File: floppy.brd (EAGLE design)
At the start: 88.6 x 93.7 mm, 19 parts, among them IC1 ATTINY13-20SU, Q1 BC547

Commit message: Changed to 96HZ, added circle on back
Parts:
- L1: value ~250nH?? -> (none)
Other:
- board text added: "96"
- board text added: "Warning: Pirate radio transmitter"
- board text removed: "91"
- board text removed: "Warning: Pirate radio transmitter / #RevoltFM"
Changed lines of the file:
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@@
 <?xml version="1.0" encoding="utf-8"?>
 <!DOCTYPE eagle SYSTEM "eagle.dtd">
-<eagle version="7.7.0">
+<eagle version="8.3.1">
 <drawing>
 <settings>
 <setting alwaysvectorfont="no"/>
+<setting keepoldvectorfont="yes"/>
 <setting verticaltext="up"/>
 </settings>
@@
 <layer number="17" name="Pads" color="2" fill="1" visible="yes" active="yes"/>
 <layer number="18" name="Vias" color="2" fill="1" visible="yes" active="yes"/>
-<layer number="19" name="Unrouted" color="6" fill="1" visible="no" active="yes"/>
+<layer number="19" name="Unrouted" color="6" fill="1" visible="yes" active="yes"/>
 <layer number="20" name="Dimension" color="15" fill="1" visible="yes" active="yes"/>
-<layer number="21" name="tPlace" color="7" fill="1" visible="yes" active="yes"/>
+<layer number="21" name="tPlace" color="7" fill="1" visible="no" active="yes"/>
 <layer number="22" name="bPlace" color="7" fill="1" visible="yes" active="yes"/>
 <layer number="23" name="tOrigins" color="15" fill="1" visible="no" active="yes"/>
-<layer number="24" name="bOrigins" color="15" fill="1" visible="no" active="yes"/>
-<layer number="25" name="tNames" color="7" fill="1" visible="yes" active="yes"/>
-<layer number="26" name="bNames" color="7" fill="1" visible="no" active="yes"/>
-<layer number="27" name="tValues" color="7" fill="1" visible="yes" active="yes"/>
+<layer number="24" name="bOrigins" color="15" fill="1" visible="yes" active="yes"/>
+<layer number="25" name="tNames" color="7" fill="1" visible="no" active="yes"/>
+<layer number="26" name="bNames" color="7" fill="1" visible="yes" active="yes"/>
+<layer number="27" name="tValues" color="7" fill="1" visible="no" active="yes"/>
 <layer number="28" name="bValues" color="7" fill="1" visible="no" active="yes"/>
-<layer number="29" name="tStop" color="7" fill="3" visible="yes" active="yes"/>
-<layer number="30" name="bStop" color="7" fill="6" visible="yes" active="yes"/>
+<layer number="29" name="tStop" color="7" fill="3" visible="no" active="yes"/>
+<layer number="30" name="bStop" color="7" fill="6" visible="no" active="yes"/>
 <layer number="31" name="tCream" color="7" fill="4" visible="no" active="yes"/>
 <layer number="32" name="bCream" color="7" fill="5" visible="no" active="yes"/>
@@
 <layer number="38" name="bTest" color="7" fill="1" visible="no" active="yes"/>
 <layer number="39" name="tKeepout" color="4" fill="11" visible="no" active="yes"/>
-<layer number="40" name="bKeepout" color="1" fill="11" visible="no" active="yes"/>
+<layer number="40" name="bKeepout" color="1" fill="11" visible="yes" active="yes"/>
 <layer number="41" name="tRestrict" color="4" fill="10" visible="no" active="yes"/>
-<layer number="42" name="bRestrict" color="1" fill="10" visible="no" active="yes"/>
+<layer number="42" name="bRestrict" color="1" fill="10" visible="yes" active="yes"/>
 <layer number="43" name="vRestrict" color="2" fill="10" visible="no" active="yes"/>
 <layer number="44" name="Drills" color="7" fill="1" visible="no" active="yes"/>
-<layer number="45" name="Holes" color="7" fill="1" visible="no" active="yes"/>
+<layer number="45" name="Holes" color="7" fill="1" visible="yes" active="yes"/>
 <layer number="46" name="Milling" color="3" fill="1" visible="no" active="yes"/>
 <layer number="47" name="Measures" color="7" fill="1" visible="no" active="yes"/>
@@
 <layer number="49" name="Reference" color="7" fill="1" visible="no" active="yes"/>
 <layer number="50" name="dxf" color="7" fill="1" visible="no" active="yes"/>
-<layer number="51" name="tDocu" color="7" fill="1" visible="yes" active="yes"/>
-<layer number="52" name="bDocu" color="7" fill="1" visible="no" active="yes"/>
+<layer number="51" name="tDocu" color="7" fill="1" visible="no" active="yes"/>
+<layer number="52" name="bDocu" color="7" fill="1" visible="yes" active="yes"/>
 <layer number="90" name="Modules" color="5" fill="1" visible="no" active="no"/>
 <layer number="91" name="Nets" color="2" fill="1" visible="no" active="no"/>
@@
 </polygon>
 <text x="6.2484" y="89.154" size="4.0132" layer="21" font="vector" ratio="16" align="center">FM</text>
-<text x="6.2738" y="84.6074" size="4.064" layer="21" font="vector" ratio="15" align="center">91</text>
+<text x="6.2738" y="84.6074" size="4.064" layer="21" font="vector" ratio="15" align="center">96</text>
 <text x="6.0706" y="80.645" size="2.54" layer="21" font="vector" ratio="17" align="center">MHz</text>
 <text x="14.097" y="38.735" size="2.54" layer="21" font="vector" ratio="15">LOADERROR</text>
@@
 <rectangle x1="1.7653" y1="92.6719" x2="2.1463" y2="92.6973" layer="22" rot="R180"/>
 <rectangle x1="1.8923" y1="92.6973" x2="2.0193" y2="92.7227" layer="22" rot="R180"/>
-<text x="44.2976" y="2.7432" size="1.7018" layer="22" font="vector" ratio="15" rot="MR0" align="center">Warning: Pirate radio transmitter / #RevoltFM</text>
+<text x="44.2976" y="2.7432" size="1.7018" layer="22" font="vector" ratio="15" rot="MR0" align="center">Warning: Pirate radio transmitter</text>
 <wire x1="11.049" y1="11.811" x2="11.049" y2="0" width="0.4064" layer="21"/>
 <wire x1="11.049" y1="5.715" x2="11.049" y2="0" width="0.4064" layer="22"/>
@@
 <dimension x1="-12.7" y1="93.98" x2="-12.7" y2="0" x3="-22.86" y3="46.99" textsize="1.778" layer="51"/>
 <dimension x1="0" y1="-7.62" x2="88.9" y2="-7.62" x3="44.45" y3="-27.94" textsize="1.778" layer="51"/>
+<circle x="44.323" y="46.863" radius="12.7" width="0.4064" layer="22"/>
 </plain>
 <attributes>
@@
 <attribute name="VALUE" x="72.39" y="29.845" size="1.27" layer="27" ratio="10" rot="R180" align="center"/>
 </element>
-<element name="L1" library="rcl" package="0207/7" value="~250nH??" x="72.39" y="48.133" smashed="yes">
+<element name="L1" library="rcl" package="0207/7" value="" x="72.39" y="48.133" smashed="yes">
 <attribute name="NAME" x="72.39" y="50.165" size="1.27" layer="25" ratio="10" align="center"/>
 <attribute name="VALUE" x="72.39" y="45.974" size="1.27" layer="27" ratio="10" align="center"/>
@@
 <attribute name="VALUE" x="64.516" y="13.0048" size="1.27" layer="27" ratio="10" rot="R180" align="center"/>
 </element>
-<element name="JP1" library="pinhead" package="1X03" value="" x="72.39" y="2.8575" rot="R180"/>
+<element name="JP1" library="pinhead" package="1X03" value="" x="72.39" y="2.8575" smashed="yes" rot="R180">
+<attribute name="VALUE" x="76.2" y="6.0325" size="1.27" layer="27" rot="R180"/>
+</element>
 <element name="TP1" library="testpad" package="B1,27" value="TPB1,27" x="86.106" y="2.54" smashed="yes">
 <attribute name="TP_SIGNAL_NAME" value="" x="85.471" y="0.635" size="1" layer="37"/>

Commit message: Changed to through-hole AVR Shortened antenna to match 96MHz
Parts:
- removed TP1: TPB1,27, testpad:B1,27
- IC1: value ATTINY13-20SU -> ATTINY13-20PU; device attiny13:SOIC8 -> attiny13:DIL08
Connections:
- net DW: no longer TP1.TP
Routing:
- net ANT: track 812.1 -> 781.7 mm
- net DW: track 15.8 -> 13.1 mm
- net GND: track 58.3 -> 60.0 mm, vias 1 -> 0
- net N$4: track 20.3 -> 19.4 mm
- net N$5: track 6.37 -> 5.74 mm

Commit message: Changed R1 to 4.7K ohm, which gives much louder sound.
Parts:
- R1: value 22K -> 4.7K
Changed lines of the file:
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@@
 </element>
 <element name="IC1" library="attiny13" package="DIL08" value="ATTINY13-20PU" x="83.185" y="8.001" smashed="yes" rot="R90"/>
-<element name="R1" library="rcl" package="0207/7" value="22K" x="64.516" y="14.986" smashed="yes" rot="R180">
+<element name="R1" library="rcl" package="0207/7" value="4.7K" x="64.516" y="14.986" smashed="yes" rot="R180">
 <attribute name="NAME" x="64.516" y="16.891" size="1.27" layer="25" ratio="10" align="center"/>
 <attribute name="VALUE" x="64.516" y="13.0048" size="1.27" layer="27" ratio="10" rot="R180" align="center"/>

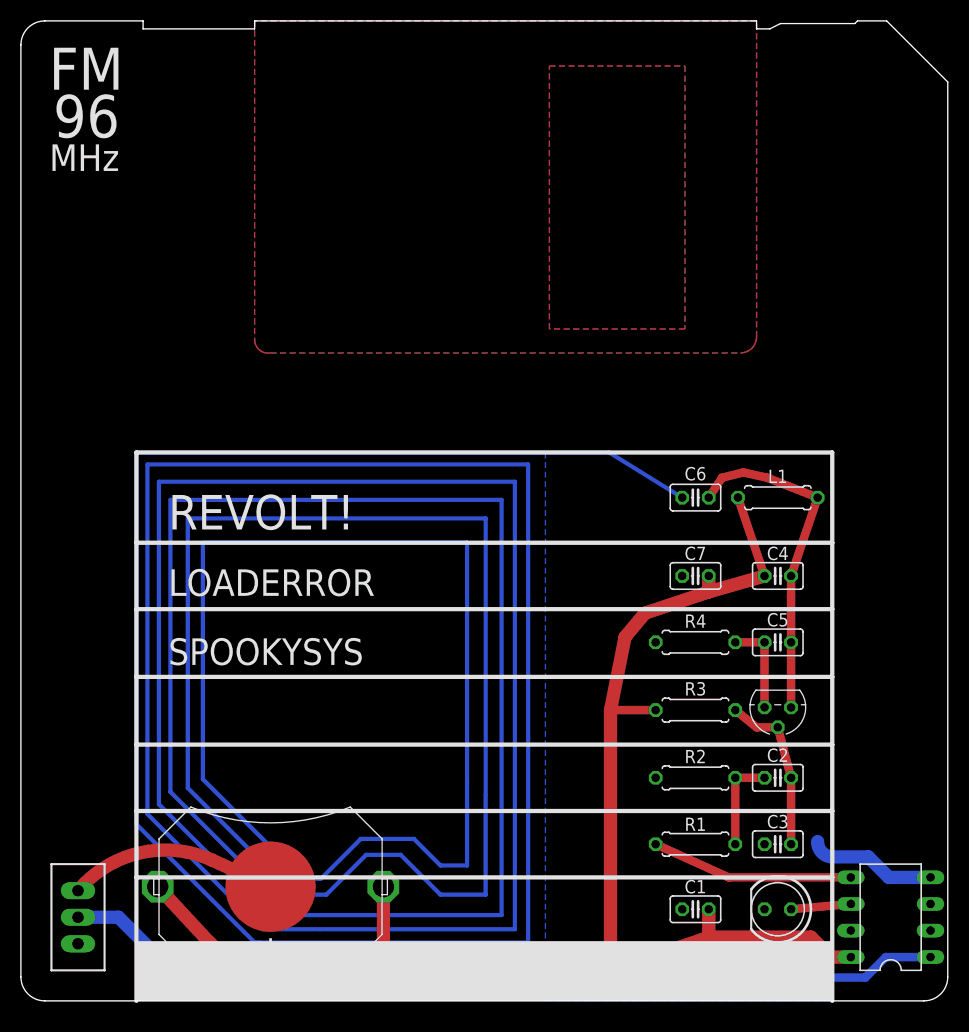
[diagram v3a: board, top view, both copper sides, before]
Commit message: Now two batteries Added inductor size too and other minor fixes
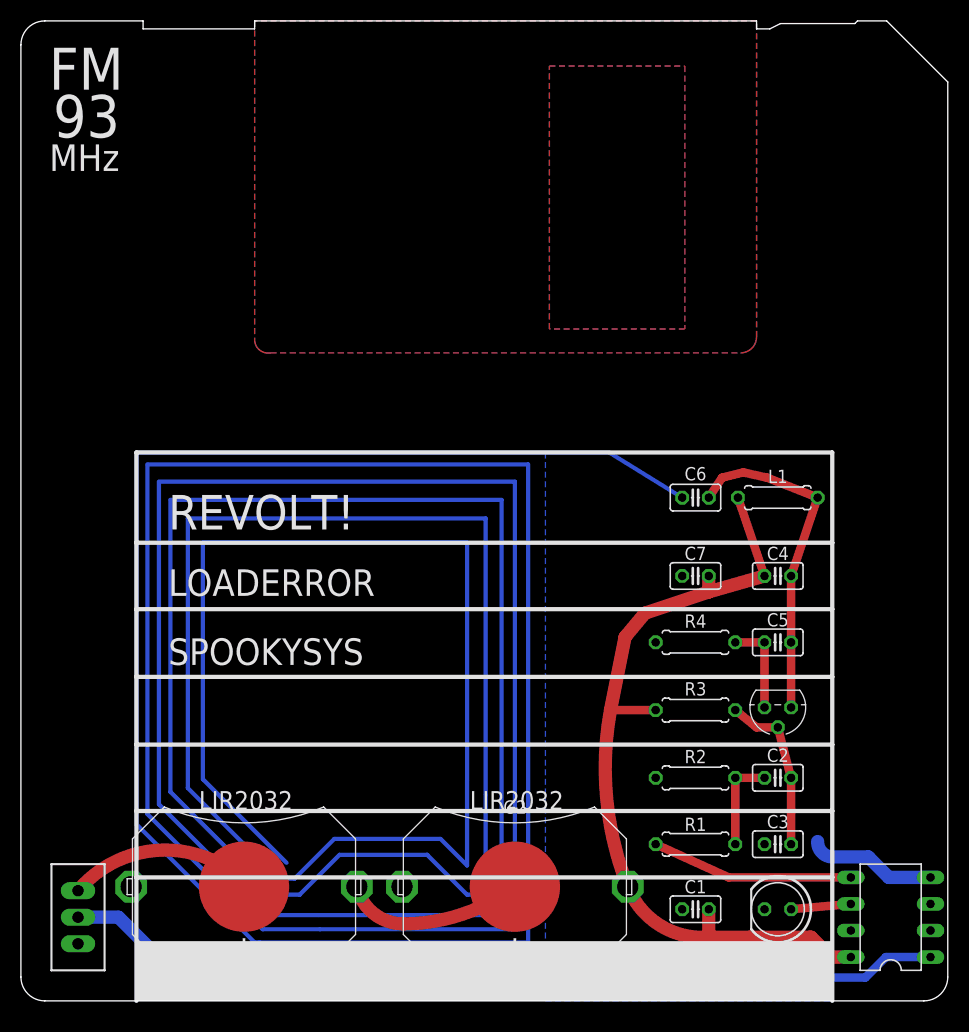
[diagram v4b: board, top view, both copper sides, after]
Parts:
- added G2: BK-913, local:BK-913
- L1: value (none) -> 62nH
- R1: value 4.7K -> 5.6K
- moved G1 2.54 mm to (21.3, 10.9)
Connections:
- new net N$9: G1.V+1, G1.V+2, G2.V-
- net VCC: now also G2.V+1, G2.V+2; no longer G1.V+1, G1.V+2
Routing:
- net VCC: track 145.2 -> 82.2 mm
- net N$9: track 0.00 -> 16.9 mm
- net N$3: track 19.3 -> 17.1 mm
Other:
- board text added: "93"
- board text added: "LIR2032"
- board text removed: "96"
